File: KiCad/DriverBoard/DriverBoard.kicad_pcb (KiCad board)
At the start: 2 copper layers, 28 x 78.1 mm, 5 parts, among them J1 Conn_01x11, J2 Conn_01x05, J4 Conn_01x12, U1 Pico

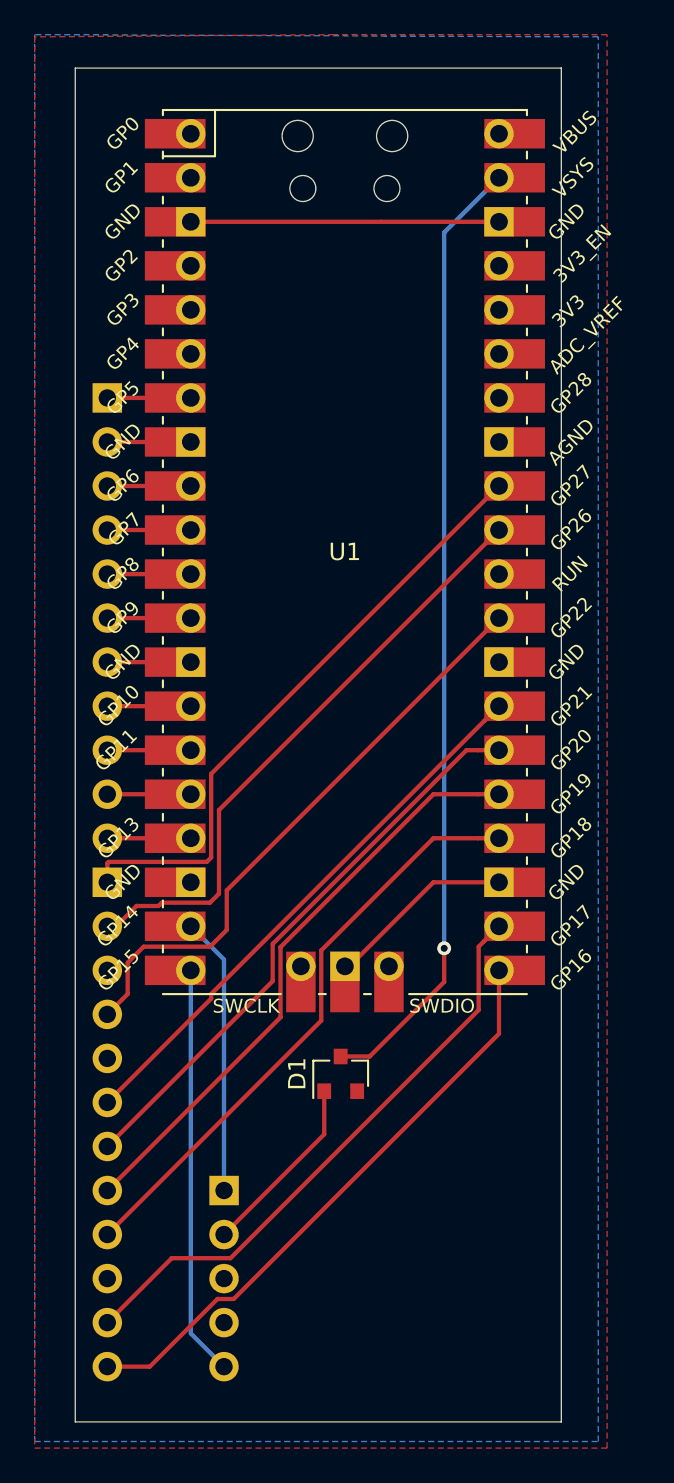
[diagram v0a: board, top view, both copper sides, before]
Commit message: Added 5V LED drivers
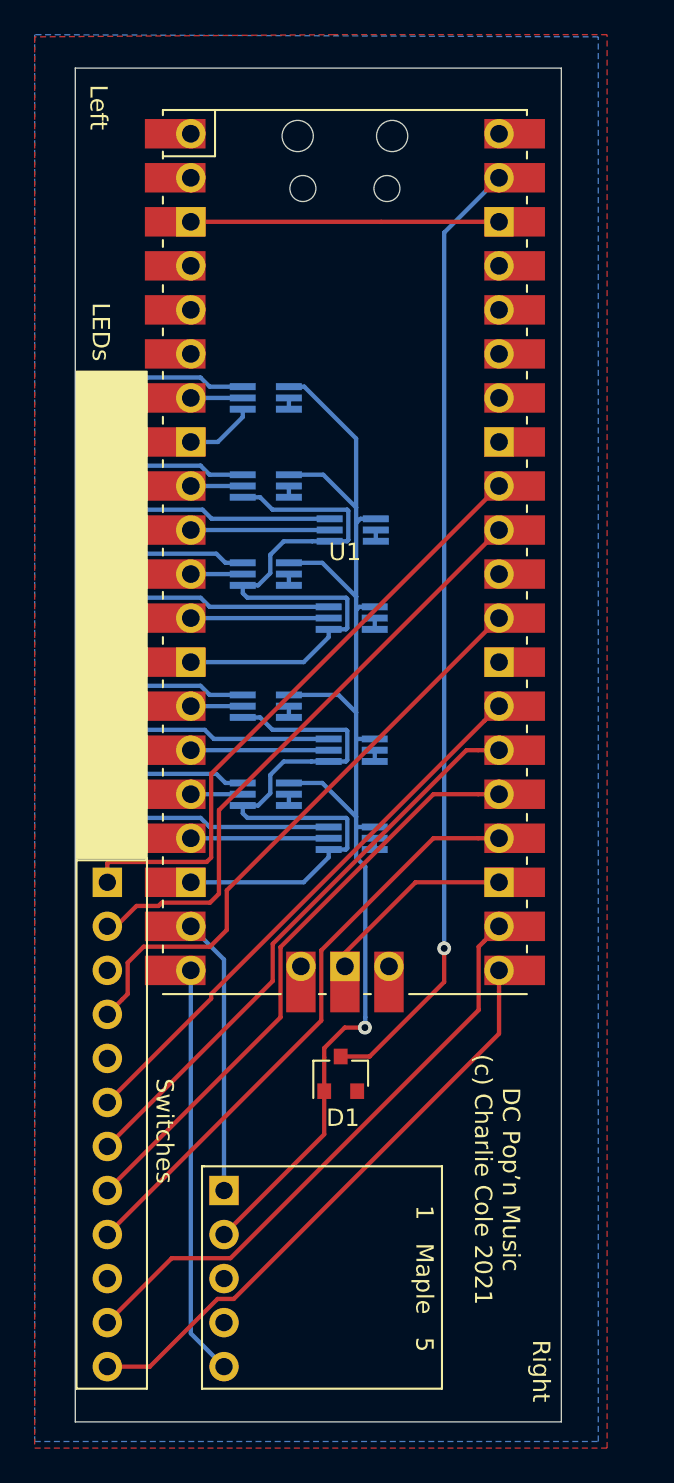
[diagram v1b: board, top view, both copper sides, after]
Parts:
- added Q1: Q_DUAL_NPN_PNP_BRT_E1B1C2E2B2C1, Package_TO_SOT_SMD:SOT-363_SC-70-6_Handsoldering, B.Cu at (66.7, 64.8)
- added Q2: Q_DUAL_NPN_PNP_BRT_E1B1C2E2B2C1, Package_TO_SOT_SMD:SOT-363_SC-70-6_Handsoldering, B.Cu at (61.7, 62.2)
- added Q3: Q_DUAL_NPN_PNP_BRT_E1B1C2E2B2C1, Package_TO_SOT_SMD:SOT-363_SC-70-6_Handsoldering, B.Cu at (66.7, 59.7)
- added Q4: Q_DUAL_NPN_PNP_BRT_E1B1C2E2B2C1, Package_TO_SOT_SMD:SOT-363_SC-70-6_Handsoldering, B.Cu at (61.7, 57.1)
- added Q5: Q_DUAL_NPN_PNP_BRT_E1B1C2E2B2C1, Package_TO_SOT_SMD:SOT-363_SC-70-6_Handsoldering, B.Cu at (66.7, 52.1)
- added Q6: Q_DUAL_NPN_PNP_BRT_E1B1C2E2B2C1, Package_TO_SOT_SMD:SOT-363_SC-70-6_Handsoldering, B.Cu at (61.7, 39.4)
- added Q7: Q_DUAL_NPN_PNP_BRT_E1B1C2E2B2C1, Package_TO_SOT_SMD:SOT-363_SC-70-6_Handsoldering, B.Cu at (61.7, 44.5)
- added Q8: Q_DUAL_NPN_PNP_BRT_E1B1C2E2B2C1, Package_TO_SOT_SMD:SOT-363_SC-70-6_Handsoldering, B.Cu at (66.7, 47.0)
- added Q9: Q_DUAL_NPN_PNP_BRT_E1B1C2E2B2C1, Package_TO_SOT_SMD:SOT-363_SC-70-6_Handsoldering, B.Cu at (61.7, 49.5)
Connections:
- J1 pad 1: LED_RIGHT_WHITE -> LED_RIGHT_WHITE_5V
- J1 pad 10: LED_LEFT_YELLOW -> LED_LEFT_YELLOW_5V
- J1 pad 11: LED_LEFT_WHITE -> LED_LEFT_WHITE_5V
- J1 pad 3: LED_RIGHT_YELLOW -> LED_RIGHT_YELLOW_5V
- J1 pad 4: LED_RIGHT_GREEN -> LED_RIGHT_GREEN_5V
- J1 pad 5: LED_RIGHT_BLUE -> LED_RIGHT_BLUE_5V
- J1 pad 6: LED_MIDDLE_RED -> LED_MIDDLE_RED_5V
- J1 pad 8: LED_LEFT_BLUE -> LED_LEFT_BLUE_5V
- J1 pad 9: LED_LEG_GREEN -> LED_LEFT_GREEN_5V
- J4 pad 3: Net-(J4-Pad3) -> (no net)
- U1 pad 15: LED_LEG_GREEN -> LED_LEFT_GREEN
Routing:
- net GND: track 38.3 -> 111.3 mm
- net +5V: track 10.7 -> 78.3 mm, vias 0 -> 1
- net LED_RIGHT_GREEN_5V: track 0.00 -> 13.5 mm
- net LED_MIDDLE_RED_5V: track 0.00 -> 13.5 mm
- net LED_LEFT_WHITE_5V: track 0.00 -> 13.5 mm
- net LED_LEFT_GREEN_5V: track 0.00 -> 13.5 mm
- net LED_LEFT_BLUE_5V: track 0.00 -> 8.52 mm
- net LED_RIGHT_BLUE_5V: track 0.00 -> 8.52 mm
- net LED_RIGHT_YELLOW_5V: track 0.00 -> 8.52 mm
- net LED_RIGHT_WHITE_5V: track 0.00 -> 8.52 mm
- net LED_LEFT_YELLOW_5V: track 0.00 -> 8.52 mm
- net LED_LEFT_GREEN: track 0.00 -> 7.95 mm
- net LED_LEG_GREEN: track 4.82 -> 0.00 mm
- net LED_RIGHT_GREEN: track 4.82 -> 8.01 mm
- net LED_MIDDLE_RED: track 4.82 -> 7.95 mm
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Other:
- board text added: "1 Maple 5"
- board text added: "5 Maple 1"
- board text added: "DC Pop’n Music (c) Charlie Cole 2021"
- board text added: "LEDs"
- board text added: "Left"
- board text added: "Right"
- board text added: "Right LEDs Left"
- board text added: "Right Switchs Left"
- board text added: "Switches"
- board text added: "github.com/charcole/ Dreamcast-PopnMusic"

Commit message: Switched misleading silkscreen and updated part numbers
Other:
- board text added: "Connectors look like they are on the back but are actually on the front! I goofed in the schematic and this was the laziest way to fix it Use right angled headers so the pins are over the Raspberry Pi Pico This is because vertical space is really tight. Connector is positioned so to avoid the tall components on the Pico like the programming button. The maple connector I soldered a right angled he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"
- board text added: "Left LEDs Right"
- board text added: "Left Switchs Right"
- board text removed: "Right LEDs Left"
- board text removed: "Right Switchs Left"
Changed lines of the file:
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@@
   (general
     (thickness 1.6)
-    (drawings 34)
+    (drawings 35)
     (tracks 222)
     (zones 0)
@@
     (40 Dwgs.User user hide)
     (41 Cmts.User user hide)
-    (42 Eco1.User user hide)
+    (42 Eco1.User user)
     (43 Eco2.User user hide)
     (44 Edge.Cuts user)
@@
     )
   )
+  (gr_text "Connectors look like they are on the back but are actually on the front!\nI goofed in the schematic and this was the laziest way to fix it\n\nUse right angled headers so the pins are over the Raspberry Pi Pico\nThis is because vertical space is really tight. Connector is positioned\nso to avoid the tall components on the Pico like the programming\nbutton.\n\nThe maple connector I soldered a right angled header upside down then\nslid off the plastic part so make a lower profile connector that can be\ninserted under the other row of connectors" (at 85.09 54.61) (layer Eco1.User)
+    (effects (font (size 1 1) (thickness 0.15) italic) (justify left))
+  )
   (gr_text "github.com/charcole/\nDreamcast-PopnMusic" (at 75.057 84.455 270) (layer B.SilkS)
     (effects (font (size 1 1) (thickness 0.15)) (justify mirror))
@@
     (effects (font (size 1 1) (thickness 0.15)))
   )
-  (gr_text "Right\n" (at 77.597 95.504 270) (layer F.SilkS)
+  (gr_text "Left\n" (at 77.597 95.504 270) (layer F.SilkS)
     (effects (font (size 1 1) (thickness 0.15)))
   )
-  (gr_text Left (at 52.07 22.606 270) (layer F.SilkS)
+  (gr_text Right (at 52.07 22.606 270) (layer F.SilkS)
     (effects (font (size 1 1) (thickness 0.15)))
   )
@@
   )
   (gr_line (start 55.372 92.456) (end 55.372 96.52) (layer B.SilkS) (width 0.12))
-  (gr_line (start 55.372 84.836) (end 55.372 87.884) (layer B.SilkS) (width 0.12))
-  (gr_line (start 55.372 75.311) (end 55.372 78.613) (layer B.SilkS) (width 0.12))
+  (gr_line (start 55.372 85.852) (end 55.372 88.9) (layer B.SilkS) (width 0.12))
+  (gr_line (start 55.372 76.708) (end 55.372 80.01) (layer B.SilkS) (width 0.12))
   (gr_line (start 55.372 71.628) (end 55.372 66.04) (layer B.SilkS) (width 0.12))
-  (gr_text "Right     Switchs     Left" (at 55.372 82.296 270) (layer B.SilkS)
+  (gr_text "Left     Switchs     Right" (at 55.372 82.296 270) (layer B.SilkS)
     (effects (font (size 1 1) (thickness 0.15)) (justify mirror))
   )
   (gr_line (start 72.009 65.913) (end 63.119 65.913) (layer B.SilkS) (width 0.12))
   (gr_line (start 72.009 63.119) (end 72.009 65.913) (layer B.SilkS) (width 0.12))
-  (gr_line (start 72.009 53.975) (end 72.009 58.42) (layer B.SilkS) (width 0.12))
-  (gr_line (start 72.009 45.212) (end 72.009 49.53) (layer B.SilkS) (width 0.12))
+  (gr_line (start 72.009 55.245) (end 72.009 59.69) (layer B.SilkS) (width 0.12))
+  (gr_line (start 72.009 46.482) (end 72.009 50.8) (layer B.SilkS) (width 0.12))
   (gr_line (start 72.009 38.1) (end 62.992 38.1) (layer B.SilkS) (width 0.12))
   (gr_line (start 72.009 41.275) (end 72.009 38.1) (layer B.SilkS) (width 0.12))
-  (gr_text "Right       LEDs       Left" (at 72.009 52.451 270) (layer B.SilkS)
+  (gr_text "Left       LEDs       Right" (at 72.009 52.451 270) (layer B.SilkS)
     (effects (font (size 1 1) (thickness 0.15)) (justify mirror))
   )
